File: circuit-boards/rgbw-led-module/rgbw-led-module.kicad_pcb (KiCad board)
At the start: 2 copper layers, 23.5 x 11.5 mm, 7 parts

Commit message: Better PCB design.
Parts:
- removed LED: GW-J9LHS1.4M_LED, bioreactor:PLCC6-RGBW-LED
- removed R_b: 9 Ohm, Resistor_SMD:R_0805_2012Metric_Pad1.20x1.40mm_HandSolder
- removed R_g: 10 Ohm, Resistor_SMD:R_0805_2012Metric_Pad1.20x1.40mm_HandSolder
- removed R_r: 19 Ohm, Resistor_SMD:R_0805_2012Metric_Pad1.20x1.40mm_HandSolder
- removed R_w: 11 Ohm, Resistor_SMD:R_0805_2012Metric_Pad1.20x1.40mm_HandSolder
- removed V+: Positive "in", Connector_PinHeader_2.54mm:PinHeader_1x04_P2.54mm_Vertical
- removed V-: Negative "out", Connector_PinHeader_2.54mm:PinHeader_1x04_P2.54mm_Vertical
- added REF**: H, Connector_PinHeader_2.54mm:PinHeader_1x04_P2.54mm_Vertical, F.Cu at (36.5, 66.0)
- added REF**: R_1206_3216Metric_Pad1.30x1.75mm_HandSolder, Resistor_SMD:R_1206_3216Metric_Pad1.30x1.75mm_HandSolder, F.Cu at (30.0, 74.6)
- added REF**: R_1206_3216Metric_Pad1.30x1.75mm_HandSolder, Resistor_SMD:R_1206_3216Metric_Pad1.30x1.75mm_HandSolder, F.Cu at (30.0, 72.2)
- added REF**: R_1206_3216Metric_Pad1.30x1.75mm_HandSolder, Resistor_SMD:R_1206_3216Metric_Pad1.30x1.75mm_HandSolder, F.Cu at (30.0, 67.8)
- added REF**: R_1206_3216Metric_Pad1.30x1.75mm_HandSolder, Resistor_SMD:R_1206_3216Metric_Pad1.30x1.75mm_HandSolder, F.Cu at (30.0, 65.4)
- added REF**: H, Connector_PinHeader_2.54mm:PinHeader_1x04_P2.54mm_Vertical, F.Cu at (23.5, 66.0)
- added REF**: LED, bioreactor:PLCC6-RGBW-LED, B.Cu at (30.0, 70.0)
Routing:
- net (no net): track 50.4 -> 85.5 mm, vias 0 -> 6
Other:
- board size 23.5 x 11.5 mm -> 20 x 20 mm
- board text added: "1"
- board text added: "2"
- board text added: "3"
- board text added: "4"

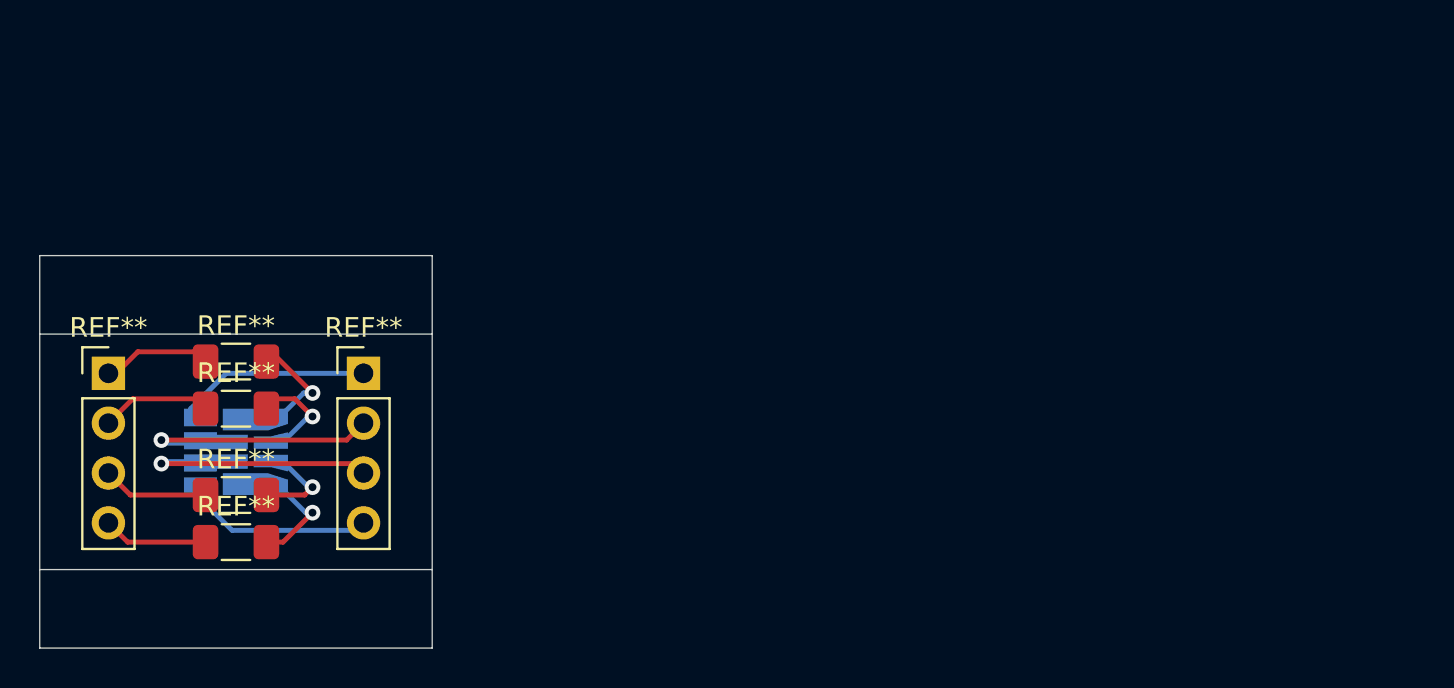
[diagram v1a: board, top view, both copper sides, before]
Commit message: Updated version of the board which actually goes through DRC checks.
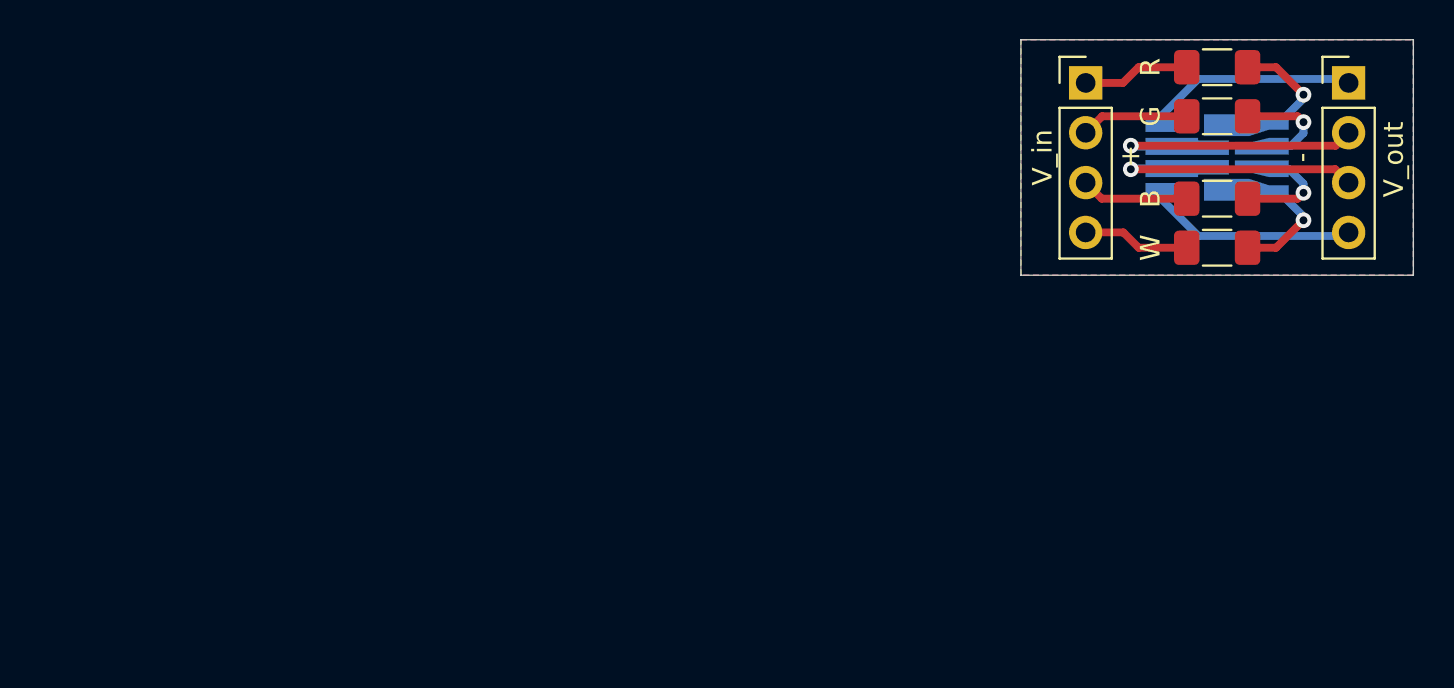
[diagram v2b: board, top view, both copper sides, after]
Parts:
- removed REF** (x2): H, Connector_PinHeader_2.54mm:PinHeader_1x04_P2.54mm_Vertical
- removed REF** (x4): R_1206_3216Metric_Pad1.30x1.75mm_HandSolder, Resistor_SMD:R_1206_3216Metric_Pad1.30x1.75mm_HandSolder
- removed REF**: LED, bioreactor:PLCC6-RGBW-LED
- added B: 9.09, Resistor_SMD:R_1206_3216Metric_Pad1.30x1.75mm_HandSolder, F.Cu at (80.0, 57.1)
- added G: 10, Resistor_SMD:R_1206_3216Metric_Pad1.30x1.75mm_HandSolder, F.Cu at (80.0, 52.9)
- added R: 19.1, Resistor_SMD:R_1206_3216Metric_Pad1.30x1.75mm_HandSolder, F.Cu at (80.0, 50.4)
- added RGBW_LED: GW+J9LHS1.4M_EN, bioreactor:RGBW_LED_GW_J9LHS1.4M_HandSolder, B.Cu at (80.0, 55.0)
- added V_in: Pin Header, Connector_PinHeader_2.54mm:PinHeader_1x04_P2.54mm_Vertical, F.Cu at (73.3, 51.2)
- added V_out: Pin Header, Connector_PinHeader_2.54mm:PinHeader_1x04_P2.54mm_Vertical, F.Cu at (86.7, 51.2)
- added W: 10, Resistor_SMD:R_1206_3216Metric_Pad1.30x1.75mm_HandSolder, F.Cu at (80.0, 59.6)
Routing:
- net (no net): track 85.5 -> 0.00 mm, vias 6 -> 0
- net Net-(GW_J9LHS1.4M1-Pad6): track 0.00 -> 12.5 mm, vias 0 -> 1
- net Net-(GW_J9LHS1.4M1-Pad7): track 0.00 -> 12.5 mm, vias 0 -> 1
- net Net-(GW_J9LHS1.4M1-Pad8): track 0.00 -> 10.9 mm
- net Net-(GW_J9LHS1.4M1-Pad5): track 0.00 -> 10.9 mm
- net Net-(R_Green1-Pad1): track 0.00 -> 5.50 mm
- net Net-(R_Blue1-Pad1): track 0.00 -> 5.49 mm
- net Net-(R_Red1-Pad1): track 0.00 -> 5.48 mm
- net Net-(R_White1-Pad1): track 0.00 -> 5.47 mm
- net Net-(GW_J9LHS1.4M1-Pad4): track 0.00 -> 5.31 mm, vias 0 -> 1
- net Net-(GW_J9LHS1.4M1-Pad1): track 0.00 -> 5.31 mm, vias 0 -> 1
- net Net-(GW_J9LHS1.4M1-Pad2): track 0.00 -> 5.00 mm, vias 0 -> 1
- net Net-(GW_J9LHS1.4M1-Pad3): track 0.00 -> 4.97 mm, vias 0 -> 1
- added copper zone on B.Cu, net (none)
- added copper zone on F.Cu, net (none)
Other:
- board size 20 x 20 mm -> 20 x 12 mm
- net class Default: trace_width 0.25 -> 0.4
- rule trace_min: 0.2 -> 0.4
- board text added: "+"
- board text added: "-"
- board text removed: "1"
- board text removed: "2"
- board text removed: "3"
- board text removed: "4"

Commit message: Remove mask clearances, because they are too loose for the LED pads.
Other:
- rule pad_to_mask_clearance: 0.05 -> 0
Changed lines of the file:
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@@
     (pad_size 1.524 1.524)
     (pad_drill 0.762)
-    (pad_to_mask_clearance 0.05)
+    (pad_to_mask_clearance 0)
     (solder_mask_min_width 0.2)
     (aux_axis_origin 0 0)
@@
     (pcbplotparams
       (layerselection 0x010fc_ffffffff)
-      (usegerberextensions false)
-      (usegerberattributes true)
-      (usegerberadvancedattributes true)
-      (creategerberjobfile true)
+      (usegerberextensions true)
+      (usegerberattributes false)
+      (usegerberadvancedattributes false)
+      (creategerberjobfile false)
       (excludeedgelayer true)
       (linewidth 0.100000)
@@
       (psa4output false)
       (plotreference true)
-      (plotvalue true)
+      (plotvalue false)
       (plotinvisibletext false)
       (padsonsilk false)
-      (subtractmaskfromsilk false)
+      (subtractmaskfromsilk true)
       (outputformat 1)
       (mirror false)
-      (drillshape 1)
+      (drillshape 0)
       (scaleselection 1)
-      (outputdirectory ""))
+      (outputdirectory "output/"))
   )
   (net 0 "")
@@
     (fp_line (start 2.45 -1.12) (end 2.45 1.12) (layer F.CrtYd) (width 0.05))
     (fp_line (start 2.45 1.12) (end -2.45 1.12) (layer F.CrtYd) (width 0.05))
-    (pad 2 smd roundrect (at 1.55 0) (size 1.3 1.75) (layers F.Cu F.Paste F.Mask) (roundrect_rratio 0.192308)
+    (pad 2 smd roundrect (at 1.55 0) (size 1.3 1.75) (layers F.Cu F.Paste F.Mask) (roundrect_rratio 0.1923076923076923)
       (net 6 "Net-(GW_J9LHS1.4M1-Pad4)"))
-    (pad 1 smd roundrect (at -1.55 0) (size 1.3 1.75) (layers F.Cu F.Paste F.Mask) (roundrect_rratio 0.192308)
+    (pad 1 smd roundrect (at -1.55 0) (size 1.3 1.75) (layers F.Cu F.Paste F.Mask) (roundrect_rratio 0.1923076923076923)
       (net 12 "Net-(R_White1-Pad1)"))
     (model ${KISYS3DMOD}/Resistor_SMD.3dshapes/R_1206_3216Metric.wrl
@@
     (fp_line (start 2.45 -1.12) (end 2.45 1.12) (layer F.CrtYd) (width 0.05))
     (fp_line (start 2.45 1.12) (end -2.45 1.12) (layer F.CrtYd) (width 0.05))
-    (pad 2 smd roundrect (at 1.55 0) (size 1.3 1.75) (layers F.Cu F.Paste F.Mask) (roundrect_rratio 0.192308)
+    (pad 2 smd roundrect (at 1.55 0) (size 1.3 1.75) (layers F.Cu F.Paste F.Mask) (roundrect_rratio 0.1923076923076923)
       (net 7 "Net-(GW_J9LHS1.4M1-Pad1)"))
-    (pad 1 smd roundrect (at -1.55 0) (size 1.3 1.75) (layers F.Cu F.Paste F.Mask) (roundrect_rratio 0.192308)
+    (pad 1 smd roundrect (at -1.55 0) (size 1.3 1.75) (layers F.Cu F.Paste F.Mask) (roundrect_rratio 0.1923076923076923)
       (net 11 "Net-(R_Red1-Pad1)"))
     (model ${KISYS3DMOD}/Resistor_SMD.3dshapes/R_1206_3216Metric.wrl
@@
     (fp_line (start 2.45 -1.12) (end 2.45 1.12) (layer F.CrtYd) (width 0.05))
     (fp_line (start 2.45 1.12) (end -2.45 1.12) (layer F.CrtYd) (width 0.05))
-    (pad 2 smd roundrect (at 1.55 0) (size 1.3 1.75) (layers F.Cu F.Paste F.Mask) (roundrect_rratio 0.192308)
+    (pad 2 smd roundrect (at 1.55 0) (size 1.3 1.75) (layers F.Cu F.Paste F.Mask) (roundrect_rratio 0.1923076923076923)
       (net 8 "Net-(GW_J9LHS1.4M1-Pad2)"))
-    (pad 1 smd roundrect (at -1.55 0) (size 1.3 1.75) (layers F.Cu F.Paste F.Mask) (roundrect_rratio 0.192308)
+    (pad 1 smd roundrect (at -1.55 0) (size 1.3 1.75) (layers F.Cu F.Paste F.Mask) (roundrect_rratio 0.1923076923076923)
       (net 1 "Net-(R_Green1-Pad1)"))
     (model ${KISYS3DMOD}/Resistor_SMD.3dshapes/R_1206_3216Metric.wrl
@@
     (fp_line (start 2.45 -1.12) (end 2.45 1.12) (layer F.CrtYd) (width 0.05))
     (fp_line (start 2.45 1.12) (end -2.45 1.12) (layer F.CrtYd) (width 0.05))
-    (pad 2 smd roundrect (at 1.55 0) (size 1.3 1.75) (layers F.Cu F.Paste F.Mask) (roundrect_rratio 0.192308)
+    (pad 2 smd roundrect (at 1.55 0) (size 1.3 1.75) (layers F.Cu F.Paste F.Mask) (roundrect_rratio 0.1923076923076923)
       (net 9 "Net-(GW_J9LHS1.4M1-Pad3)"))
-    (pad 1 smd roundrect (at -1.55 0) (size 1.3 1.75) (layers F.Cu F.Paste F.Mask) (roundrect_rratio 0.192308)
+    (pad 1 smd roundrect (at -1.55 0) (size 1.3 1.75) (layers F.Cu F.Paste F.Mask) (roundrect_rratio 0.1923076923076923)
       (net 10 "Net-(R_Blue1-Pad1)"))
     (model ${KISYS3DMOD}/Resistor_SMD.3dshapes/R_1206_3216Metric.wrl
